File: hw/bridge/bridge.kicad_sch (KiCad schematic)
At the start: 43 parts, among them J1 USB_C_Receptacle_USB2.0_14P, J2 DE9, U1 CH340E, U2 MAX485E, U3 CH334R, U4 74LVC2G04, U5 MCP1754S-3302xCB, U6 TJA1051T-3, Y1 HCI XC53G2-12.000-F20LJDT

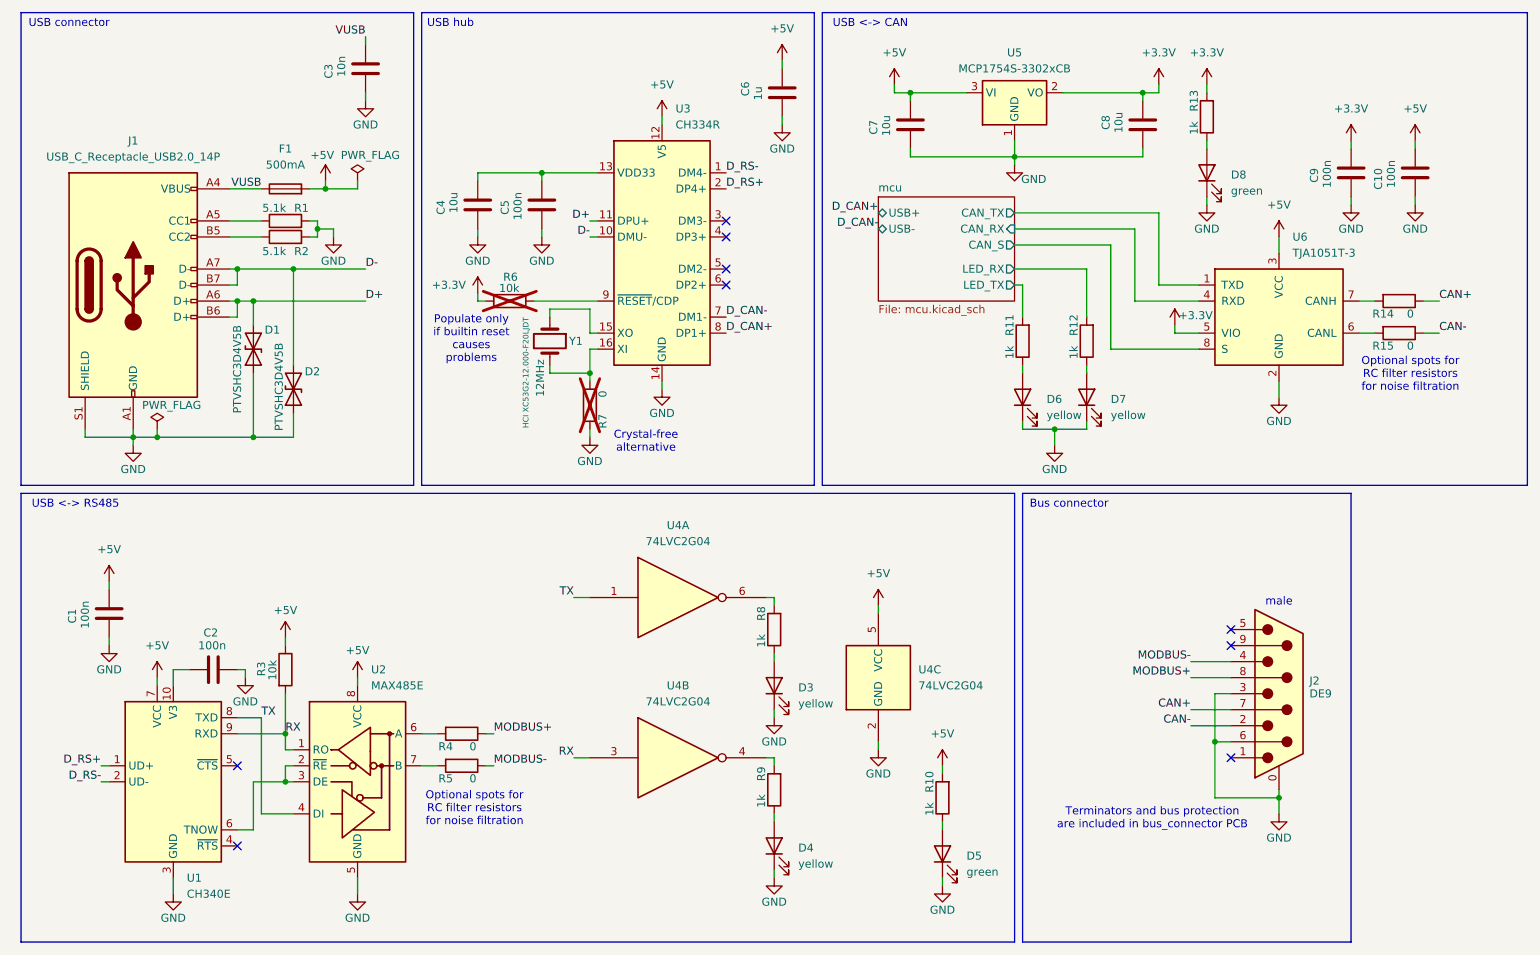
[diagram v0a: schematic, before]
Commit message: Manufacture fixes
Signed-off-by: Mateusz Pająk <22417805+Tai-Min@users.noreply.github.com>
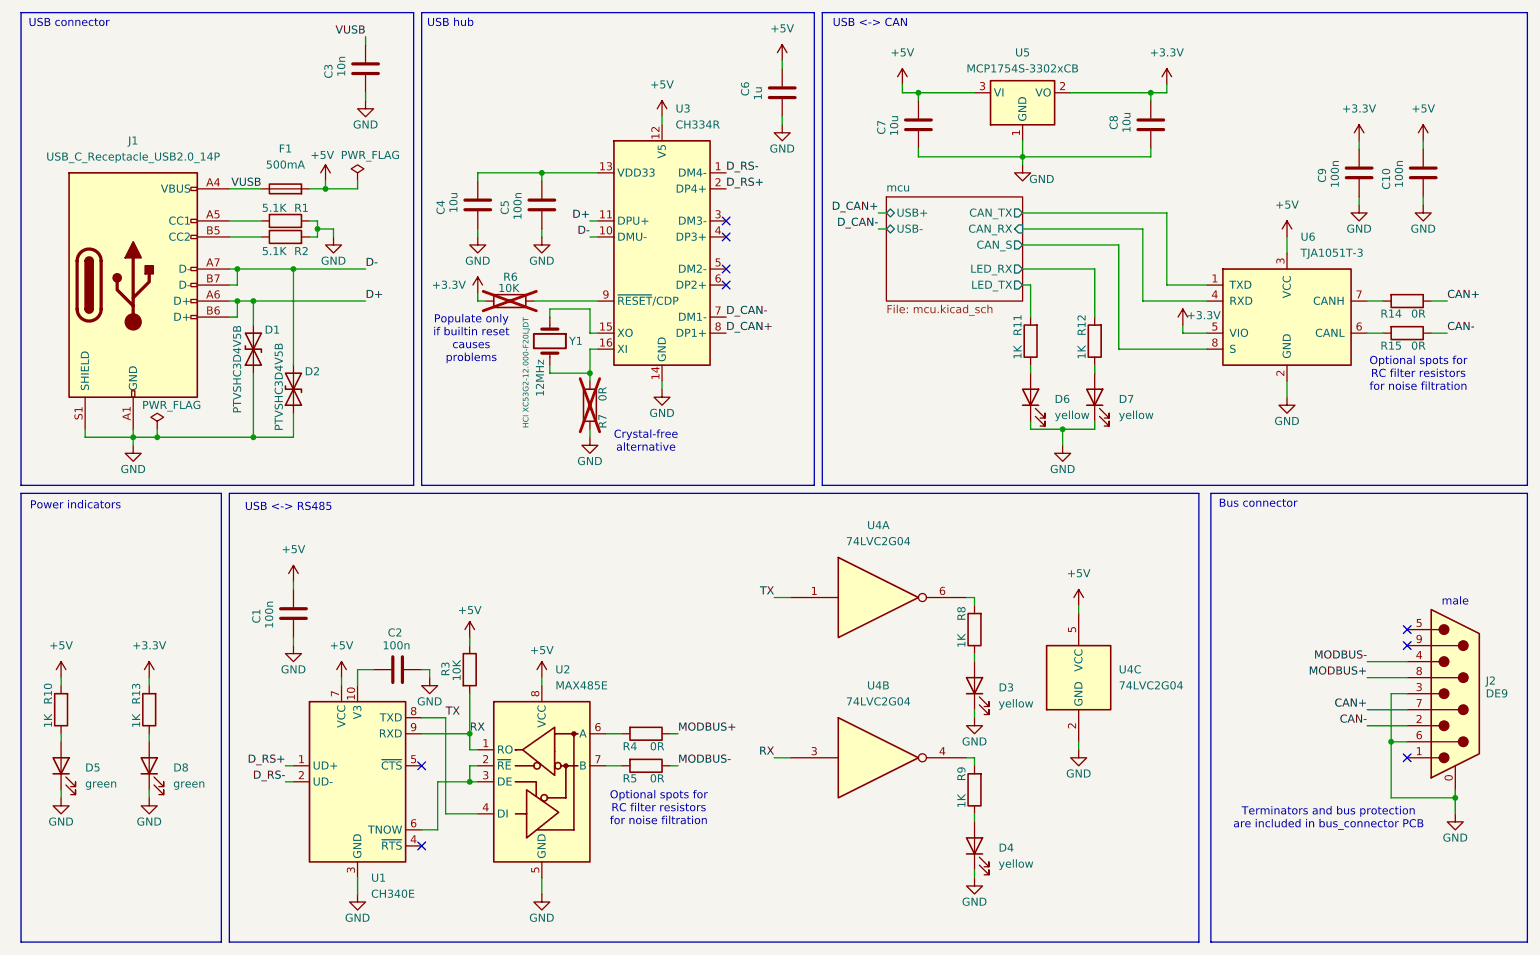
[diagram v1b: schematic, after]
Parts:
- R1, R2: value 5.1k -> 5.1K
- R10, R11, R12, R13, R8, R9: value 1k -> 1K
- R14, R15, R4, R5, R7: value 0 -> 0R
- R3, R6: value 10k -> 10K
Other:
- note added: "Power indicators"
- moved on the sheet: C1, C10, C2, C7, C8, C9, D3, D4, D5, D6, D7, D8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
